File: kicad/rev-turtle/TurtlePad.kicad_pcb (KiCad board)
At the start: 2 copper layers, 57.2 x 63.6 mm, 40 parts, among them J1 USB_IN, J2 AVR-ISP-6, SW1 SW_Push, U1 USBLC6-2SC6, U2 ATMEGA32U4, Y1 16MHz

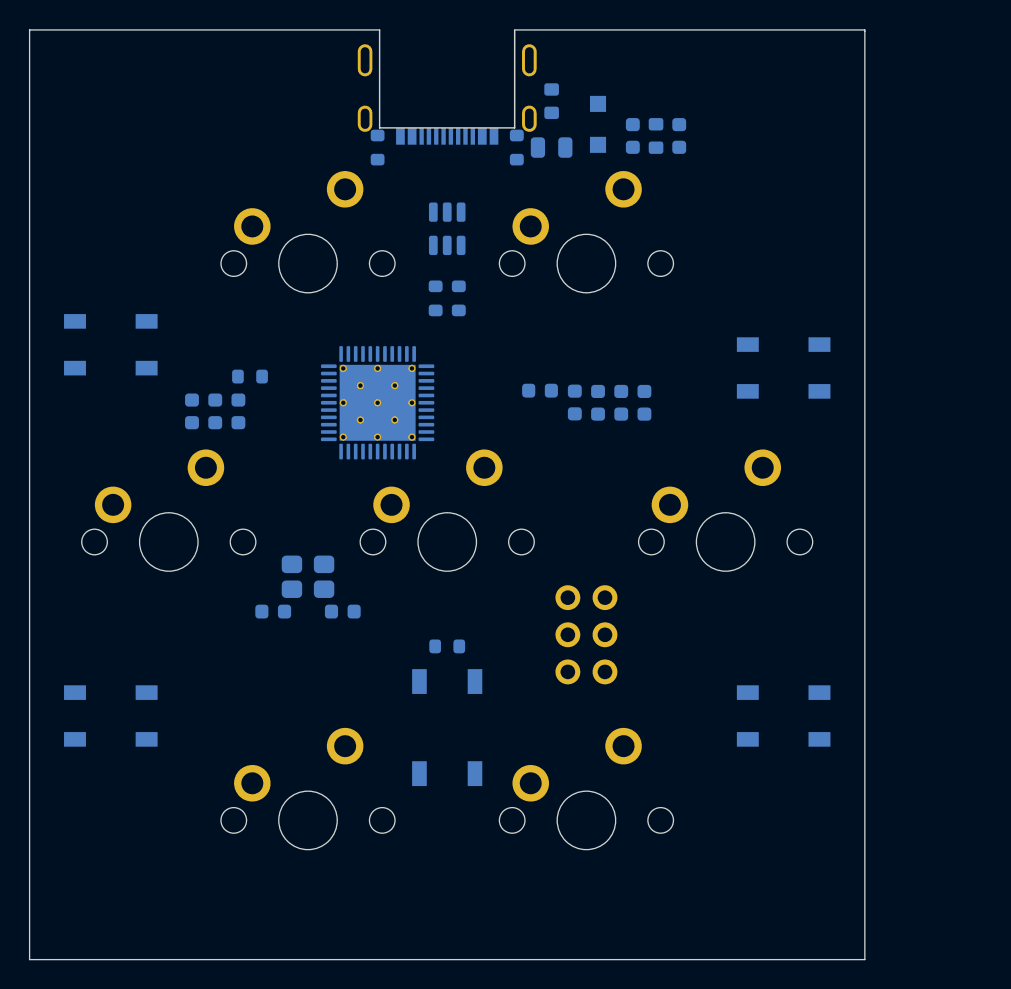
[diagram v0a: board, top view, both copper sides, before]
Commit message: Redid schematic because I am an idiot
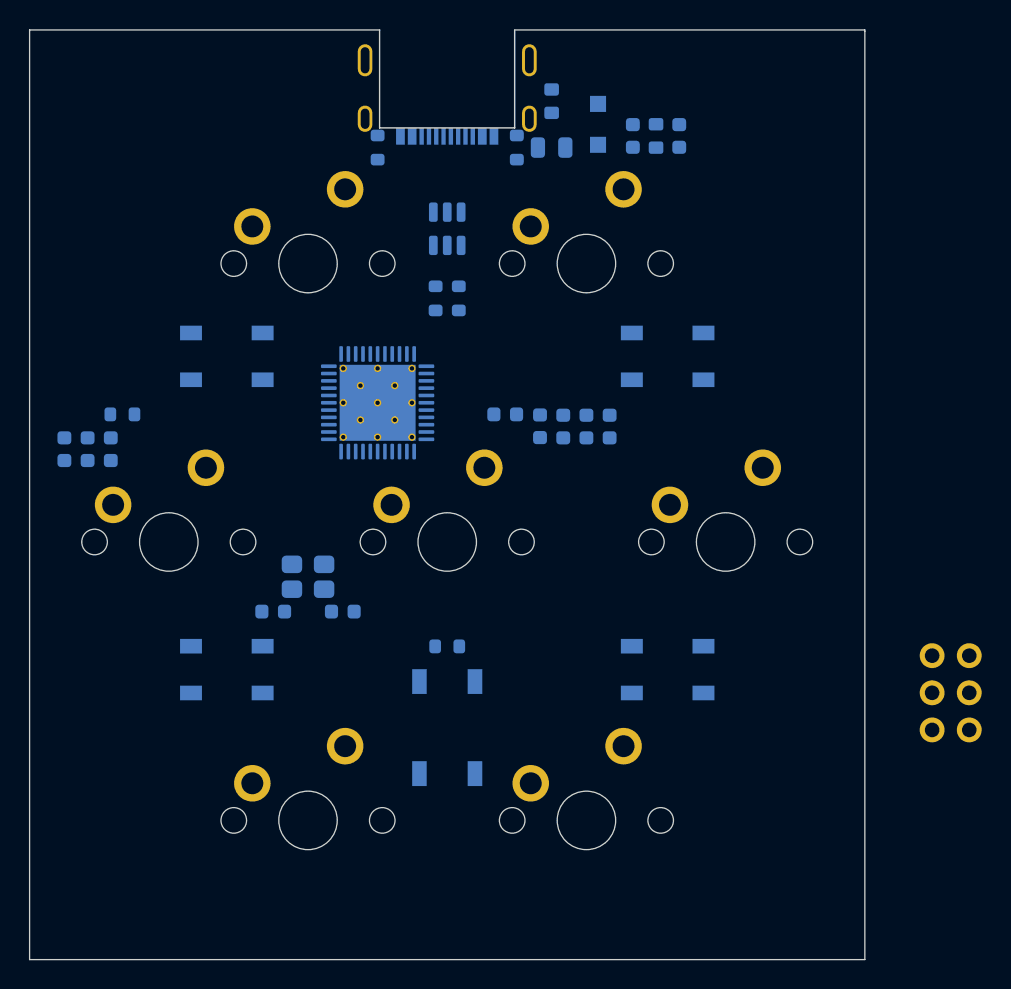
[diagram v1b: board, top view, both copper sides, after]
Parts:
- moved J2 25.2 mm to (162.2, 100.1)
- moved C10 9.11 mm to (101.6, 83.4)
- moved C9 9.11 mm to (103.2, 83.4)
- moved R6 9.11 mm to (105.6, 81.0)
- moved C11 9.11 mm to (104.8, 83.4)
- moved RGB2 8.55 mm to (112.7, 98.5)
- moved RGB3 8.55 mm to (142.9, 98.5), turned to 0 degrees
- moved RGB1 7.98 mm to (112.7, 77.1), turned to 0 degrees
- moved RGB4 7.98 mm to (142.9, 77.1), turned to 0 degrees
- moved C12 2.88 mm to (131.8, 81.0)
- moved C4 2.88 mm to (135.7, 81.9)
- moved C3 2.88 mm to (137.3, 81.9)
- moved C5 2.88 mm to (134.1, 81.9)
- moved C6 2.88 mm to (138.9, 81.9)
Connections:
- C12 pad 1: Net-(C12-Pad1) -> VCC
- C9 pad 1: VCC -> Net-(C9-Pad1)
- J2 pad 3: S3 -> SCK
- U2 pad 12: MX4 -> unconnected-(U2-Pad12)
- U2 pad 18: MX6 -> MX1
- U2 pad 19: MX7 -> MX2
- U2 pad 20: unconnected-(U2-Pad20) -> MX3
- U2 pad 21: unconnected-(U2-Pad21) -> MX4
- U2 pad 22: unconnected-(U2-Pad22) -> MX6
- U2 pad 25: unconnected-(U2-Pad25) -> MX5
- U2 pad 26: unconnected-(U2-Pad26) -> MX7
- U2 pad 28: MX1 -> unconnected-(U2-Pad28)
- U2 pad 29: MX2 -> unconnected-(U2-Pad29)
- U2 pad 30: MX3 -> unconnected-(U2-Pad30)
- U2 pad 31: MX5 -> unconnected-(U2-Pad31)
- U2 pad 6: Net-(C12-Pad1) -> Net-(C9-Pad1)
- U2 pad 8: RGB -> LED
- U2 pad 9: unconnected-(U2-Pad9) -> SCK
